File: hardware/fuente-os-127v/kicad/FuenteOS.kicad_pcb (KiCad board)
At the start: 2 copper layers, 50 x 50 mm, 14 parts, among them J1 127 VCA, J2 SALIDA OS

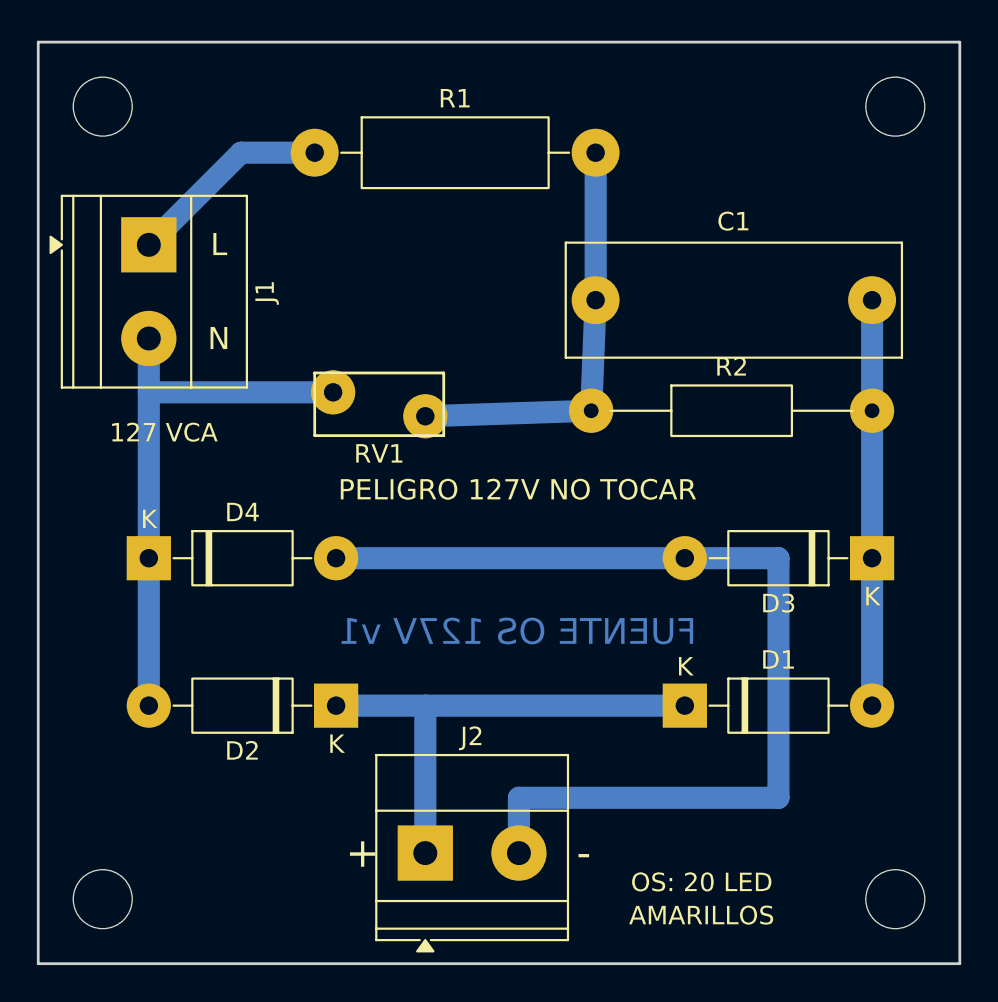
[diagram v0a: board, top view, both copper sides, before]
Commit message: Placa OS v2 (27 LED, puente 2W10, capacitor paso 10/15 mm) y secuenciador de flechas 127 VCA
- fuente-os-127v: O (13) + S (14) = 27 LED; C1 334J -> 10 mA (474J si son blanco
  calido); puente redondo 2W10; huella de capacitor con barrenos a 10 y 15 mm.
- flechas-127v: NE555 + CD4017 + 3 SCR MCR100-6, dos fuentes capacitivas con
  2W10 (logica 474J + zener 12 V, flechas 224J ~8 mA). PCB 50x60 mm una cara,
  2 puentes de alambre; ERC/DRC 0 con paridad; PDF 1:1 para planchar, Gerber,
  Excellon, BOM.
- gen/comun.py: huellas, esquema, PCB, ruteo y separacion de redes por puentes
  compartidos por ambas placas.

Co-Authored-By: Claude Opus 5.5 <noreply@anthropic.com>
Claude-Session: https://claude.ai/code/session_01WVk3oGwfQfGTmAT2PMp8oW
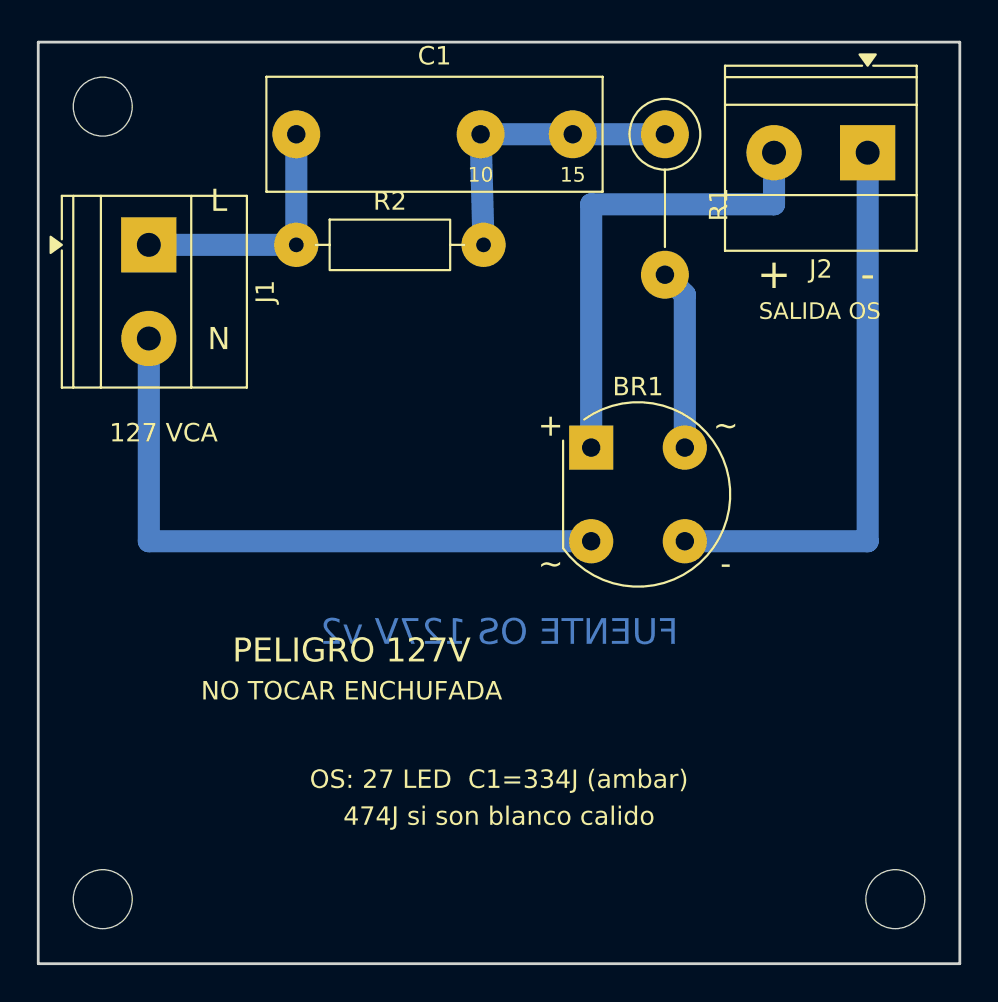
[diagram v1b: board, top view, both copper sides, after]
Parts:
- removed D1, D2, D3, D4: 1N4007, FuenteOS:D_DO-41_P10.16mm
- removed H4: MountingHole_3.2mm_M3, FuenteOS:Barreno_M3_3.2mm
- removed RV1: 07D201K, FuenteOS:Varistor_D7mm_P5mm
- added BR1: 2W10, FuenteOS:Puente_2W10, F.Cu at (130.0, 122.0)
- C1: footprint FuenteOS:C_Poliester_P15mm -> FuenteOS:C_Poliester_P10-15mm
- R1: footprint FuenteOS:R_1W_P15.24mm -> FuenteOS:R_1W_Vertical_P7.62mm
- R2: footprint FuenteOS:R_Axial_P15.24mm -> FuenteOS:R_Axial_P10.16mm
- moved H2 60.8 mm to (103.5, 146.5)
- moved J2 44.9 mm to (145.0, 106.0), turned to 180 degrees
- moved H3 43.0 mm to (146.5, 146.5)
- moved R1 19.0 mm to (134.0, 105.0), turned to -90 degrees
- moved C1 18.6 mm to (114.0, 105.0)
- moved R2 18.4 mm to (114.0, 111.0)
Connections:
- C1 pad 1: /A -> /L
- C1 pad 2: /AC1 -> /X
- J2 pad 1: /OS+ -> /OS-
- J2 pad 2: /OS- -> /OS+
- R1 pad 1: /L -> /X
- R1 pad 2: /A -> /AC
- R2 pad 1: /A -> /L
- R2 pad 2: /AC1 -> /X
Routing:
- net /OS-: track 54.1 -> 31.0 mm
- net /A: track 23.0 -> 0.00 mm
- net /AC1: track 22.0 -> 0.00 mm
- net /X: track 0.00 -> 16.0 mm
- net /AC: track 0.00 -> 9.83 mm
- net /N: track 29.9 -> 35.0 mm
- net /L: track 11.1 -> 14.0 mm
- net /OS+: track 26.9 -> 25.9 mm
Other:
- board text added: "474J si son blanco calido"
- board text added: "FUENTE OS 127V v2"
- board text added: "NO TOCAR ENCHUFADA"
- board text added: "OS: 27 LED C1=334J (ambar)"
- board text added: "PELIGRO 127V"
- board text added: "SALIDA OS"
- board text removed: "AMARILLOS"
- board text removed: "FUENTE OS 127V v1"
- board text removed: "OS: 20 LED"
- board text removed: "PELIGRO 127V NO TOCAR"
